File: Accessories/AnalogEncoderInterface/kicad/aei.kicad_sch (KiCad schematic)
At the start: 58 parts, among them J1 Screw_Terminal_01x06, J2 1935161, J3 Screw_Terminal_01x06, J4 RJ45, U1 INA2143U, U2 INA2143U, U3 LT1764EQ-1.5-PBF

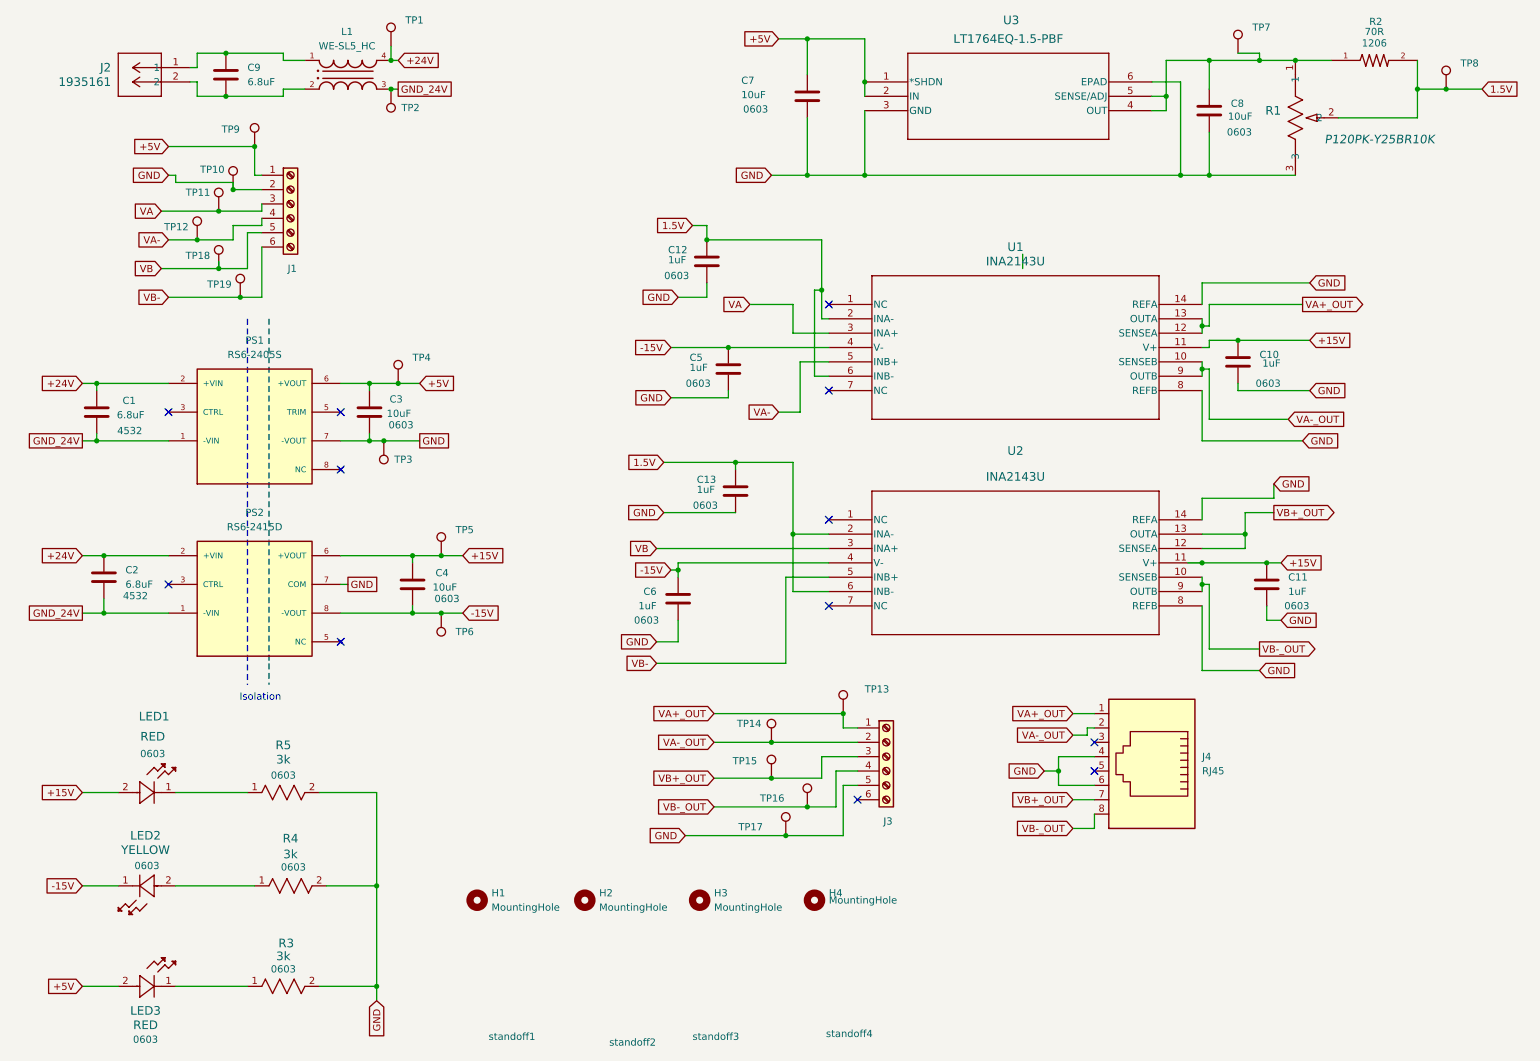
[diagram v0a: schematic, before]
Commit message: Update schematic to match naming convention
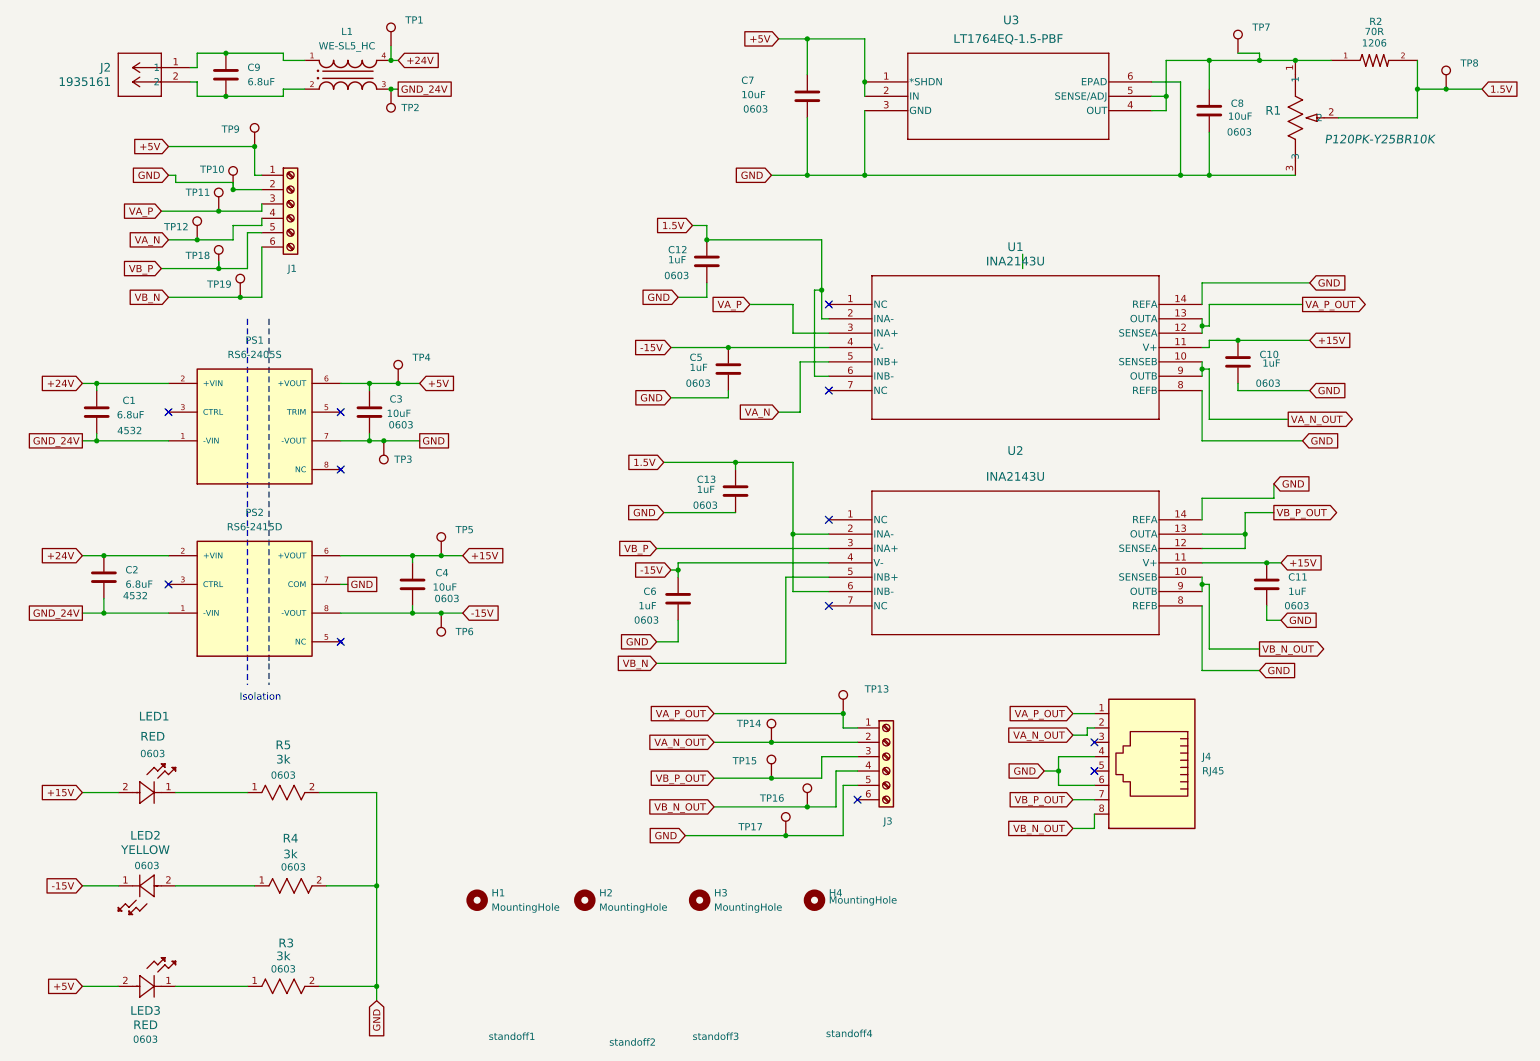
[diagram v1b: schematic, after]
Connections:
- net VA renamed VA_P
- net VA+_OUT renamed VA_P_OUT
- net VA- renamed VA_N
- net VA-_OUT renamed VA_N_OUT
- net VB renamed VB_P
- net VB+_OUT renamed VB_P_OUT
- net VB- renamed VB_N
- net VB-_OUT renamed VB_N_OUT
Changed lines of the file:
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@@
 	)
 	(junction
-		(at 237.49 110.49)
-		(diameter 0)
-		(color 0 0 0 0)
-	)
-	(junction
 		(at 82.55 21.59)
 		(diameter 0)
@@
 	)
 	(junction
-		(at 86.36 119.38)
+		(at 237.49 110.49)
 		(diameter 0)
 		(color 0 0 0 0)
 	)
 	(junction
-		(at 153.67 105.41)
+		(at 86.36 119.38)
 		(diameter 0)
 		(color 0 0 0 0)
 	)
 	(junction
-		(at 269.24 26.67)
+		(at 153.67 105.41)
 		(diameter 0)
 		(color 0 0 0 0)
 	)
 	(junction
-		(at 226.06 110.49)
+		(at 269.24 26.67)
 		(diameter 0)
 		(color 0 0 0 0)
@@
 	(wire
 		(pts
-			(xy 223.52 110.49) (xy 226.06 110.49)
-		)
-		(stroke
-			(width 0)
-			(type default)
-		)
-	)
-	(wire
-		(pts
 			(xy 55.88 63.5) (xy 59.69 63.5)
 		)
@@
 	(wire
 		(pts
-			(xy 226.06 110.49) (xy 237.49 110.49)
-		)
-		(stroke
-			(width 0)
-			(type default)
-		)
-	)
-	(wire
-		(pts
 			(xy 133.35 120.65) (xy 133.35 124.46)
 		)
@@
 	(wire
 		(pts
+			(xy 226.06 110.49) (xy 237.49 110.49)
+		)
+		(stroke
+			(width 0)
+			(type default)
+		)
+	)
+	(wire
+		(pts
 			(xy 156.21 31.75) (xy 156.21 41.91)
 		)
@@
 		)
 	)
-	(global_label "VA+_OUT"
+	(global_label "VA_P_OUT"
 		(shape output)
 		(at 243.84 64.77 0)
@@
 		)
 		(property "Intersheetrefs" "${INTERSHEET_REFS}"
-			(at 255.171 64.77 0)
+			(at 255.8362 64.77 0)
 			(effects
 				(font
@@
 		)
 	)
-	(global_label "VA+_OUT"
+	(global_label "VA_P_OUT"
 		(shape input)
 		(at 139.7 137.16 180)
@@
 		)
 		(property "Intersheetrefs" "${INTERSHEET_REFS}"
-			(at 128.369 137.16 0)
+			(at 127.7038 137.16 0)
 			(effects
 				(font
@@
 		)
 	)
-	(global_label "VA"
+	(global_label "VA_P"
 		(shape input)
 		(at 41.91 48.26 180)
@@
 		)
 		(property "Intersheetrefs" "${INTERSHEET_REFS}"
-			(at 36.7476 48.26 0)
+			(at 34.51 48.26 0)
 			(effects
 				(font
@@
 		)
 	)
-	(global_label "VA+_OUT"
+	(global_label "VA_P_OUT"
 		(shape input)
 		(at 203.2 137.16 180)
@@
 		)
 		(property "Intersheetrefs" "${INTERSHEET_REFS}"
-			(at 191.869 137.16 0)
+			(at 191.2038 137.16 0)
 			(effects
 				(font
@@
 		)
 	)
-	(global_label "VB-_OUT"
+	(global_label "VB_N_OUT"
 		(shape input)
 		(at 139.7 153.67 180)
@@
 		)
 		(property "Intersheetrefs" "${INTERSHEET_REFS}"
-			(at 128.1876 153.67 0)
+			(at 127.4619 153.67 0)
 			(effects
 				(font
@@
 		)
 	)
-	(global_label "VA-_OUT"
+	(global_label "VA_N_OUT"
 		(shape input)
 		(at 139.7 142.24 180)
@@
 		)
 		(property "Intersheetrefs" "${INTERSHEET_REFS}"
-			(at 128.369 142.24 0)
+			(at 127.6433 142.24 0)
 			(effects
 				(font
@@
 		)
 	)
-	(global_label "VB+_OUT"
+	(global_label "VB_P_OUT"
 		(shape output)
 		(at 238.76 101.6 0)
@@
 		)
 		(property "Intersheetrefs" "${INTERSHEET_REFS}"
-			(at 250.2724 101.6 0)
+			(at 250.9376 101.6 0)
 			(effects
 				(font
@@
 		)
 	)
-	(global_label "VB"
+	(global_label "VB_P"
 		(shape input)
 		(at 41.91 58.42 180)
@@
 		)
 		(property "Intersheetrefs" "${INTERSHEET_REFS}"
-			(at 36.5662 58.42 0)
+			(at 34.3286 58.42 0)
 			(effects
 				(font
@@
 		)
 	)
-	(global_label "VB-_OUT"
+	(global_label "VB_N_OUT"
 		(shape input)
 		(at 203.2 157.48 180)
@@
 		)
 		(property "Intersheetrefs" "${INTERSHEET_REFS}"
-			(at 191.6876 157.48 0)
+			(at 190.9619 157.48 0)
 			(effects
 				(font
@@
 		)
 	)
-	(global_label "VA-"
+	(global_label "VA_N"
 		(shape input)
 		(at 151.13 83.82 180)
@@
 		)
 		(property "Intersheetrefs" "${INTERSHEET_REFS}"
-			(at 144.3952 83.82 0)
+			(at 143.6695 83.82 0)
 			(effects
 				(font
@@
 		)
 	)
-	(global_label "VA-_OUT"
-		(shape input)
+	(global_label "VA_N_OUT"
+		(shape output)
 		(at 241.3 85.09 0)
 		(fields_autoplaced yes)
@@
 		)
 		(property "Intersheetrefs" "${INTERSHEET_REFS}"
-			(at 252.631 85.09 0)
+			(at 253.3567 85.09 0)
 			(effects
 				(font
@@
 		)
 	)
-	(global_label "VA-_OUT"
+	(global_label "VA_N_OUT"
 		(shape input)
 		(at 203.2 140.97 180)
@@
 		)
 		(property "Intersheetrefs" "${INTERSHEET_REFS}"
-			(at 191.869 140.97 0)
+			(at 191.1433 140.97 0)
 			(effects
 				(font
@@
 		)
 	)
-	(global_label "VB"
+	(global_label "VB_P"
 		(shape input)
 		(at 129.54 107.95 180)
@@
 		)
 		(property "Intersheetrefs" "${INTERSHEET_REFS}"
-			(at 124.1962 107.95 0)
+			(at 121.9586 107.95 0)
 			(effects
 				(font
@@
 		)
 	)
-	(global_label "VA"
+	(global_label "VA_P"
 		(shape input)
 		(at 146.05 64.77 180)
@@
 		)
 		(property "Intersheetrefs" "${INTERSHEET_REFS}"
-			(at 140.8876 64.77 0)
+			(at 138.65 64.77 0)
 			(effects
 				(font
@@
 		)
 	)
-	(global_label "VB+_OUT"
+	(global_label "VB_P_OUT"
 		(shape input)
 		(at 139.7 148.59 180)
@@
 		)
 		(property "Intersheetrefs" "${INTERSHEET_REFS}"
-			(at 128.1876 148.59 0)
+			(at 127.5224 148.59 0)
 			(effects
 				(font
@@
 		)
 	)
-	(global_label "VA-"
+	(global_label "VA_N"
 		(shape input)
 		(at 43.18 53.34 180)
@@
 		)
 		(property "Intersheetrefs" "${INTERSHEET_REFS}"
-			(at 36.4452 53.34 0)
+			(at 35.7195 53.34 0)
 			(effects
 				(font
@@
 		)
 	)
-	(global_label "VB+_OUT"
+	(global_label "VB_P_OUT"
 		(shape input)
 		(at 203.2 152.4 180)
@@
 		)
 		(property "Intersheetrefs" "${INTERSHEET_REFS}"
-			(at 191.6876 152.4 0)
+			(at 191.0224 152.4 0)
 			(effects
 				(font
@@
 		)
 	)
-	(global_label "VB-"
+	(global_label "VB_N"
 		(shape input)
 		(at 43.18 63.5 180)
@@
 		)
 		(property "Intersheetrefs" "${INTERSHEET_REFS}"
-			(at 36.2638 63.5 0)
+			(at 35.5381 63.5 0)
 			(effects
 				(font
@@
 		)
 	)
-	(global_label "VB-_OUT"
+	(global_label "VB_N_OUT"
 		(shape output)
 		(at 236.22 125.73 0)
@@
 		)
 		(property "Intersheetrefs" "${INTERSHEET_REFS}"
-			(at 247.7324 125.73 0)
+			(at 248.4581 125.73 0)
 			(effects
 				(font
@@
 		)
 	)
-	(global_label "VB-"
+	(global_label "VB_N"
 		(shape input)
 		(at 129.54 128.27 180)
@@
 		)
 		(property "Intersheetrefs" "${INTERSHEET_REFS}"
-			(at 122.6238 128.27 0)
+			(at 121.8981 128.27 0)
 			(effects
 				(font
